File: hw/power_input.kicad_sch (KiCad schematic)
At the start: 24 parts, among them Q101 SQD50P08-25L, Q102 IPD90N10S4-06, U101 TLV3201, U102 UCC27517A

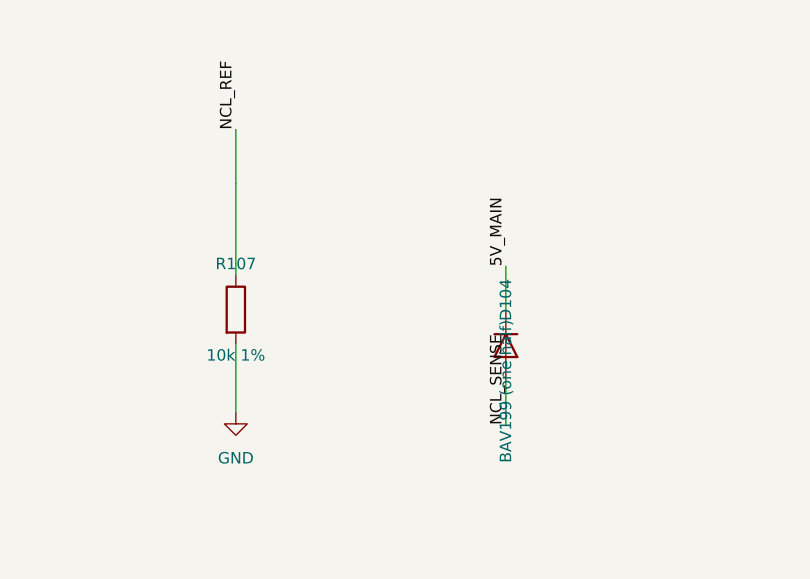
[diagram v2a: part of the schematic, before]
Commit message: Replace the analog-input zeners with BAV199-Q rail clamps
LOWV-CLAMP, analog half. The ten 3.3 V zeners on the sensor and cam
inputs leaked at signal level (the datasheet allows 5 uA at 1 V); they
are now BAV199-Q (80 nA max at 150 C, AEC-Q101) to 3V3_MCU and ground,
drawn as one 3-pin part so each pair is one package. The speed input's
split BAV199 halves and the power-input sense clamp use the same part.

A rail clamp needs something the zener did not: the BAV199's upper
diode is high-Vf, so on a 40 V harness short the MCU pad's ESD diode
would take most of the fault current, over the +/-3 mA injection
limit. Each clamped channel now has 1k between clamp and pad: 0.40 mA
injected. sensor_ratiometric and cam_frontend model the pair, the 1k
and the pad diode, and check the injection current.

The new models also showed the old zener loading the cam signal by
84 mV at a 5.25 V rail -- pinned by the old check as the expected
value. Re-pinned to the divider's own 3.231 V.

The discrete inputs stay open: they clamp continuously, which neither
a rail clamp nor an LM4040-class reference (35 uA bias below
breakdown) can do within the pin's ratings.

24/24 sim blocks, netlist gate passing, 197 R/C packaged.
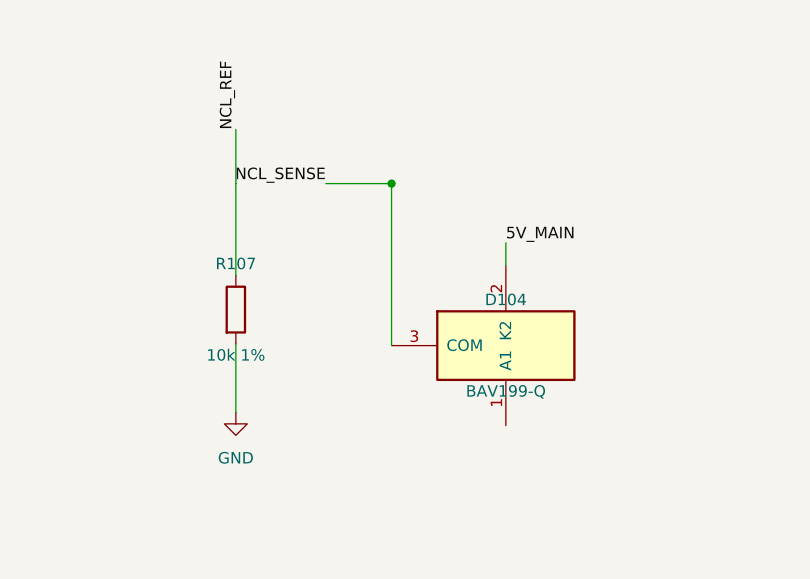
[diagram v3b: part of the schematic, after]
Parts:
- removed D104: BAV199 (one half), symbol Device:D
- added D104: BAV199-Q, Package_TO_SOT_SMD:SOT-23, symbol ecu25kva:BAV199
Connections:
- net 5V_MAIN: now also D104.2 (K2)
- net NCL_SENSE: now also D104.3 (COM)
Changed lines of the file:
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@@
     )
   )
-  (symbol (lib_id "Device:D") (at 190.0 256.0 270) (unit 1)
+  (label "NCL_SENSE" (at 170.0 238.0 180)
+    (effects (font (size 1.27 1.27)) (justify right bottom))
+  )
+  (symbol (lib_id "ecu25kva:BAV199") (at 190.0 256.0 0) (unit 1)
     (in_bom yes) (on_board yes) (fields_autoplaced)
     (property "Reference" "D104" (id 0) (at 190.0 250.92 0)
       (effects (font (size 1.27 1.27)))
     )
-    (property "Value" "BAV199 (one half)" (id 1) (at 190.0 261.08 0)
+    (property "Value" "BAV199-Q" (id 1) (at 190.0 261.08 0)
       (effects (font (size 1.27 1.27)))
     )
-    (property "Footprint" "" (id 2) (at 190.0 256.0 0)
+    (property "Footprint" "Package_TO_SOT_SMD:SOT-23" (id 2) (at 190.0 256.0 0)
       (effects (font (size 1.27 1.27)) hide)
     )
@@
       (effects (font (size 1.27 1.27)) hide)
     )
-    (property "Tag" "VR-CLAMP" (id 4) (at 190.0 256.0 0)
+    (property "MPN" "BAV199-Q" (id 4) (at 190.0 256.0 0)
       (effects (font (size 1.27 1.27)) hide)
     )
-    (property "Note" "Anode to the sense node, cathode to 5V_MAIN: holds the comparator input inside its rail when VIN is at 73.3 V. LOW LEAKAGE for the same reason as on the crank input -- and here leakage lifts the sense node, which makes the clamp release EARLIER, the safe direction." (id 5) (at 190.0 256.0 0)
+    (property "Tag" "VR-CLAMP" (id 5) (at 190.0 256.0 0)
+      (effects (font (size 1.27 1.27)) hide)
+    )
+    (property "Note" "Common pin on the sense node, K2 to 5V_MAIN: holds the comparator input inside its rail when VIN is at 73.3 V. A1 OPEN -- the lower diode would clamp the negative excursion the comparator exists to see. Leakage lifts the sense node, which makes the clamp release EARLIER, the safe direction." (id 6) (at 190.0 256.0 0)
       (effects (font (size 1.27 1.27)) hide)
     )
   )
-  (wire (pts (xy 190.0 252.19) (xy 190.0 247.19))
+  (wire (pts (xy 170.0 238.0) (xy 177.3 238.0))
     (stroke (width 0) (type default))
   )
-  (label "5V_MAIN" (at 190.0 247.19 90)
+  (junction (at 177.3 238.0) (diameter 0) (color 0 0 0 0)
+  )
+  (wire (pts (xy 177.3 238.0) (xy 177.3 256.0))
+    (stroke (width 0) (type default))
+  )
+  (wire (pts (xy 190.0 247.11) (xy 190.0 244.57))
+    (stroke (width 0) (type default))
+  )
+  (label "5V_MAIN" (at 190.0 244.57 0)
     (effects (font (size 1.27 1.27)) (justify left bottom))
   )
-  (wire (pts (xy 190.0 259.81) (xy 190.0 264.81))
-    (stroke (width 0) (type default))
-  )
-  (label "NCL_SENSE" (at 190.0 264.81 270)
-    (effects (font (size 1.27 1.27)) (justify left bottom))
-  )

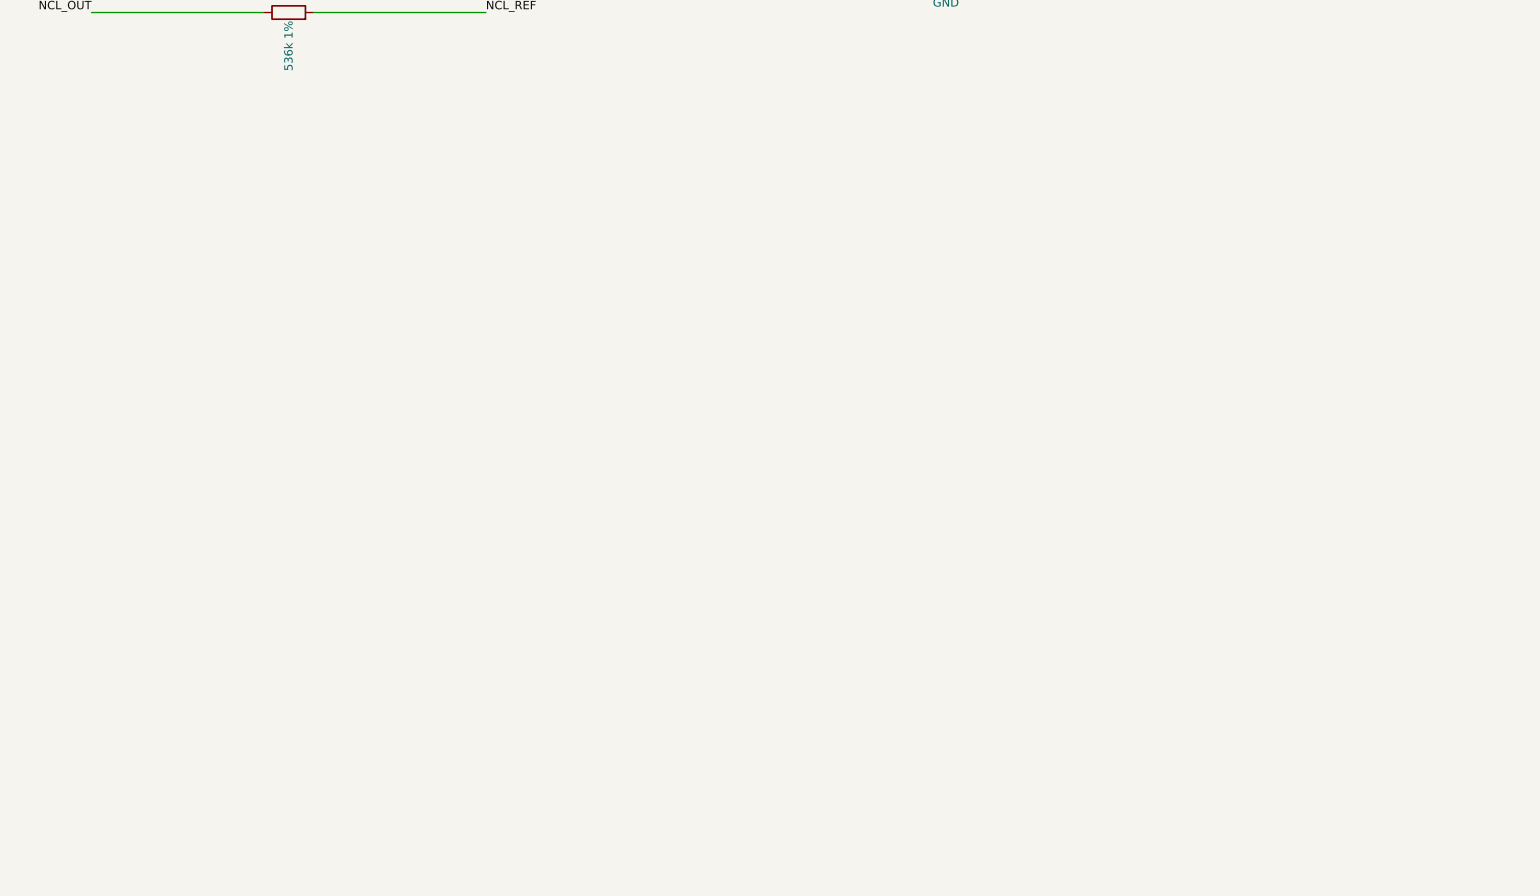
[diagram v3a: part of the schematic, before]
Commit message: Move the injector and EGR supply onto pins 04 and 06 (POWER-PATH)
Every high-current load drew through pin 21, whose reverse FET was
sized for 5 A and whose EMI filter never stated a DC current. Pin 04
now feeds VBAT_INJ (the injector hold switches and the boost power
stage), and pin 06 feeds VBAT_EGR (the EGR bridge). Each is fused 10 A
in the loom and has its own SMCJ43CA TVS, SQM120P10-10m1L reverse
P-FET (passive gate, as Q1), SS20PH102HM3 backstop and 2 x 2.2 uF.
Pin 21 keeps the buck, the relays, the metering freewheel and the
boost controller's VDD.

The pin-21 FET could not simply be copied: at the EGR's 6.4 A stall it
would pass its junction limit on a 105 C board. The new part, from
Vishay doc 76943 Rev. A, runs at Tj 139 C (155 C cranking) on the EGR
rail and 117 C on the injector rail. The new block power_path.cir
holds those figures as 18 checks. check_netlist now fails unless each
rail leaves its own FET for its own loads and VBAT_PROT reaches
neither power stage.

The sheets are generated against KiCad 7.0.11's symbol library, which
regenerates an unchanged sheet identically. KiCad 10's library would
have rewritten every embedded symbol.

Gates: 25/25 blocks; connectivity OK with the same 2 open items; 333
components, 314 with footprints; 208 passives packaged. The questions
put to the owner -- the split, the reverse protection, what stays on
pin 21, and the KiCad/ngspice choices -- are in decisions-log.md
sections 5 and 6. The spec, the BOM requirements, the handbook, status
and the handoff are updated to match, and the bible is rebuilt (333
pages).
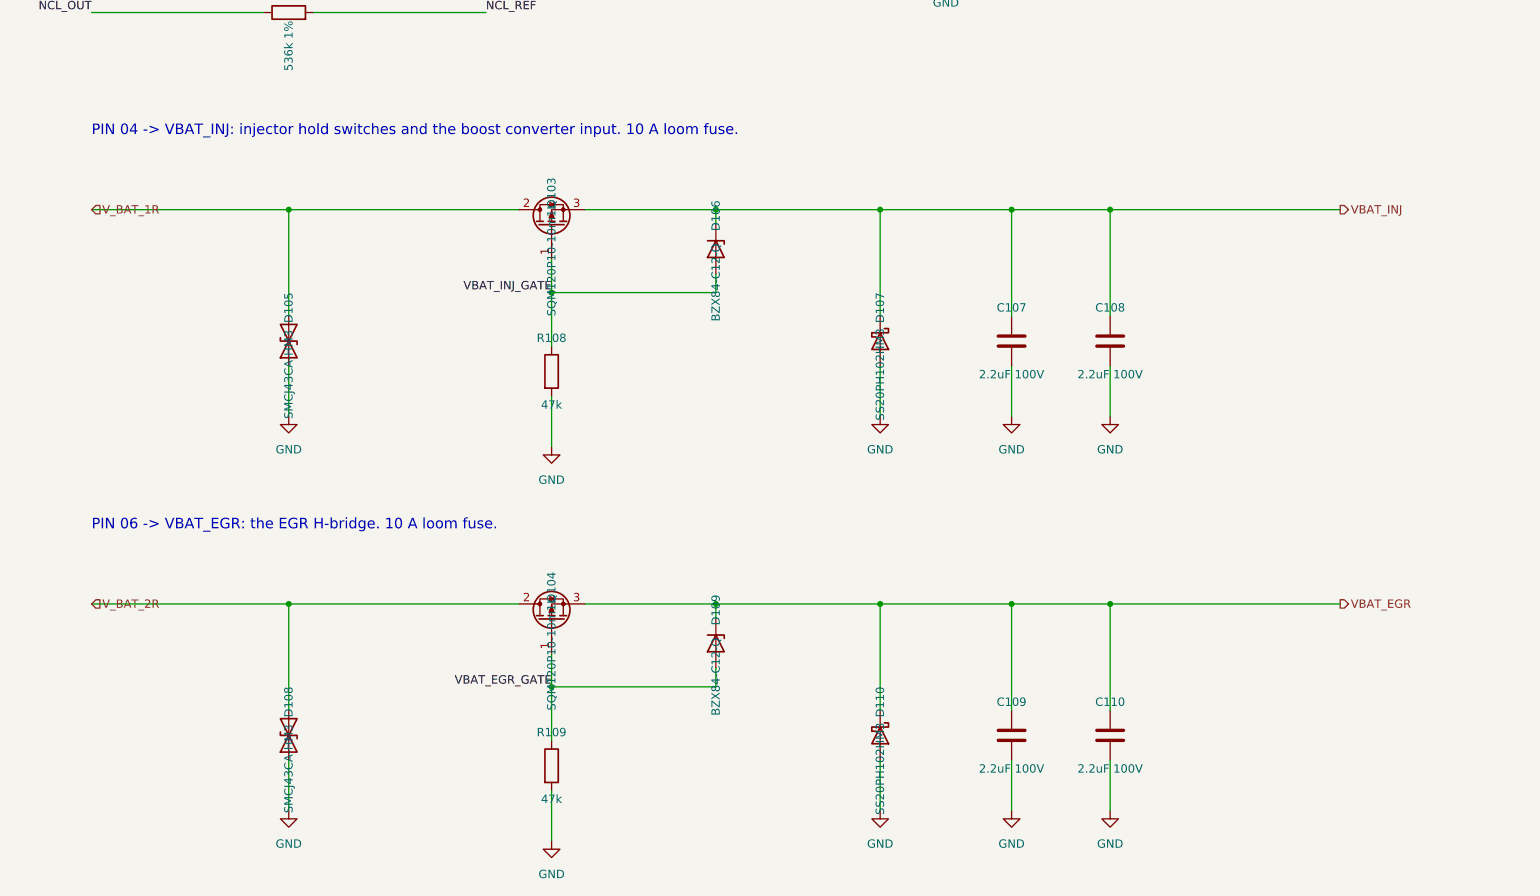
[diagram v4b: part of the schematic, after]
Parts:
- added C107, C108, C109, C110: 2.2uF 100V, Capacitor_SMD:C_1210_3225Metric, symbol Device:C
- added D105, D108: SMCJ43CA-HM3, Diode_SMD:D_SMC, symbol Device:D_TVS
- added D106, D109: BZX84-C12-Q, ecu25kva:SOT-23_Zener_K1_A2, symbol Device:D_Zener
- added D107, D110: SS20PH102HM3, ecu25kva:TO-277A_K1_A2, symbol Device:D_Schottky
- added Q103, Q104: SQM120P10-10m1L, Package_TO_SOT_SMD:TO-263-2, symbol Device:Q_PMOS_GDS
- added R108, R109: 47k, Resistor_SMD:R_0805_2012Metric, symbol Device:R
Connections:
- net GND: now also C107.2, C108.2, C109.2, C110.2, D105.1 (A1), D107.2 (A), D108.1 (A1), D110.2 (A), R108.2, R109.2
- new net VBAT_EGR: C109.1, C110.1, D109.1 (K), D110.1 (K), Q104.3 (S)
- new net VBAT_EGR_GATE: D109.2 (A), Q104.1 (G), R109.1
- new net VBAT_INJ: C107.1, C108.1, D106.1 (K), D107.1 (K), Q103.3 (S)
- new net VBAT_INJ_GATE: D106.2 (A), Q103.1 (G), R108.1
- new net V_BAT_1R: D105.2 (A2), Q103.2 (D)
- new net V_BAT_2R: D108.2 (A2), Q104.2 (D)
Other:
- note added: "PIN 04 -> VBAT_INJ: injector hold switches and the boost converter input. 10 A loom fuse."
- note added: "PIN 06 -> VBAT_EGR: the EGR H-bridge. 10 A loom fuse."

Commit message: Choose pin 21's filter inductors and fuse for its post-POWER-PATH load
With the injector and EGR gone, pin 21 carries at most 2.95 A. That is
an upper bound, not an estimate. The LM5164's IPEAK1 maximum of 1.75 A
(SNVSAU4D) caps the buck's average input current whatever the 5 V load
is. The rest is the two relay coils at 24 V (0.30 A), the metering
freewheel (0.86 A) and the boost VDD feed (0.04 A).

  L101  Wurth 7447709220, 22 uH WE-PD: Isat 6.5 A typ, 117 C at the
        bound on a 105 C board (max 125 C)
  L102  Wurth 744314047, 0.47 uH WE-HCI 7050: Isat 9 A typ
  F101  Littelfuse 0437005.WRA, 5 A 63 V 437A (was 20 A): 3.16 A at
        105 C, 1.07x over the bound

The EMI model now carries both inductors' RDC and self-resonance, and
Lf is 0.47 uH. The 150 and 400 kHz margins fell to 0.56 and 0.73 dB
against the existing placeholder gates. F101's pulse I2t is computed
from the simulated waveforms: pulse 1 is 16% of melting, pulse 2a is
2.5%. The 20% ceiling for the repeated pulse is a rule of thumb, and
the BOM requirements say so. Both land patterns were checked against
the Wurth drawings.

Gates: 25/25 blocks, connectivity OK, 317 of 333 with footprints, 208
passives unchanged. The bible is rebuilt (334 pages).
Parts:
- F101: value 20A -> 0437005.WRA; footprint (none) -> Fuse:Fuse_1206_3216Metric; Chosen (none) -> Littelfuse 437A, 1206 fast-acting, 63 V DC, 50 A interrupti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; Class (none) -> 5A; MPN (none) -> 0437005.WRA; Source spec sec.2.2 -- OEM harness fuse 8F1 class -> run_sim.py emi_filter (pin 21 load), transient_clamp and ne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
- L101: value 22uH -> 7447709220; footprint (none) -> Inductor_SMD:L_Wuerth_WE-PD-Typ-LS; Chosen (none) -> Wurth WE-PD 1210, 22 uH, IR 5.3 A, Isat 6.5 A typ, 28 mOhm 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; Class (none) -> 22uH; MPN (none) -> 7447709220; Source emi_filter.cir L1 -> emi_filter.cir L1 -- RDC and self-resonance modelled
- L102: value 0.5uH -> 744314047; footprint (none) -> Inductor_SMD:L_Wuerth_HCI-7050; Chosen (none) -> Wurth WE-HCI 7050, 0.47 uH, IR 18 A, Isat 9 A typ, 1.35 mOh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; Class (none) -> 0.47uH; MPN (none) -> 744314047; Source emi_filter.cir Lf -> emi_filter.cir Lf -- RDC and self-resonance modelled
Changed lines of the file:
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@@
       (effects (font (size 1.27 1.27)))
     )
-    (property "Value" "20A" (id 1) (at 52 85.08 0)
+    (property "Value" "0437005.WRA" (id 1) (at 52 85.08 0)
       (effects (font (size 1.27 1.27)))
     )
-    (property "Footprint" "" (id 2) (at 52 80.0 0)
+    (property "Footprint" "Fuse:Fuse_1206_3216Metric" (id 2) (at 52 80.0 0)
       (effects (font (size 1.27 1.27)) hide)
     )
@@
       (effects (font (size 1.27 1.27)) hide)
     )
-    (property "Source" "spec sec.2.2 -- OEM harness fuse 8F1 class" (id 4) (at 52 80.0 0)
+    (property "MPN" "0437005.WRA" (id 4) (at 52 80.0 0)
+      (effects (font (size 1.27 1.27)) hide)
+    )
+    (property "Class" "5A" (id 5) (at 52 80.0 0)
+      (effects (font (size 1.27 1.27)) hide)
+    )
+    (property "Chosen" "Littelfuse 437A, 1206 fast-acting, 63 V DC, 50 A interrupting, melting I2t 2.30 A2s, AEC-Q200. 3.16 A continuous at 105 C" (id 6) (at 52 80.0 0)
+      (effects (font (size 1.27 1.27)) hide)
+    )
+    (property "Source" "run_sim.py emi_filter (pin 21 load), transient_clamp and negative_pulses (pulse I2t)" (id 7) (at 52 80.0 0)
       (effects (font (size 1.27 1.27)) hide)
     )
@@
       (effects (font (size 1.27 1.27)))
     )
-    (property "Value" "22uH" (id 1) (at 80 85.08 0)
+    (property "Value" "7447709220" (id 1) (at 80 85.08 0)
       (effects (font (size 1.27 1.27)))
     )
-    (property "Footprint" "" (id 2) (at 80 80.0 0)
+    (property "Footprint" "Inductor_SMD:L_Wuerth_WE-PD-Typ-LS" (id 2) (at 80 80.0 0)
       (effects (font (size 1.27 1.27)) hide)
     )
@@
       (effects (font (size 1.27 1.27)) hide)
     )
-    (property "Source" "emi_filter.cir L1" (id 4) (at 80 80.0 0)
+    (property "MPN" "7447709220" (id 4) (at 80 80.0 0)
+      (effects (font (size 1.27 1.27)) hide)
+    )
+    (property "Class" "22uH" (id 5) (at 80 80.0 0)
+      (effects (font (size 1.27 1.27)) hide)
+    )
+    (property "Chosen" "Wurth WE-PD 1210, 22 uH, IR 5.3 A, Isat 6.5 A typ, 28 mOhm max, SRF 10 MHz, 120 V, AEC-Q200 Grade 1. Land pattern checked against the datasheet's: 2.9 x 5.4 pads, 7.0 gap" (id 6) (at 80 80.0 0)
+      (effects (font (size 1.27 1.27)) hide)
+    )
+    (property "Source" "emi_filter.cir L1 -- RDC and self-resonance modelled" (id 7) (at 80 80.0 0)
       (effects (font (size 1.27 1.27)) hide)
     )
@@
       (effects (font (size 1.27 1.27)))
     )
-    (property "Value" "0.5uH" (id 1) (at 138 85.08 0)
+    (property "Value" "744314047" (id 1) (at 138 85.08 0)
       (effects (font (size 1.27 1.27)))
     )
-    (property "Footprint" "" (id 2) (at 138 80.0 0)
+    (property "Footprint" "Inductor_SMD:L_Wuerth_HCI-7050" (id 2) (at 138 80.0 0)
       (effects (font (size 1.27 1.27)) hide)
     )
@@
       (effects (font (size 1.27 1.27)) hide)
     )
-    (property "Source" "emi_filter.cir Lf" (id 4) (at 138 80.0 0)
+    (property "MPN" "744314047" (id 4) (at 138 80.0 0)
       (effects (font (size 1.27 1.27)) hide)
     )
+    (property "Class" "0.47uH" (id 5) (at 138 80.0 0)
+      (effects (font (size 1.27 1.27)) hide)
+    )
+    (property "Chosen" "Wurth WE-HCI 7050, 0.47 uH, IR 18 A, Isat 9 A typ, 1.35 mOhm, SRF 235 MHz, AEC-Q200 Grade 1. Land pattern checked: 2.7 x 2.2 pads, 2.4 gap" (id 6) (at 138 80.0 0)
+      (effects (font (size 1.27 1.27)) hide)
+    )
+    (property "Source" "emi_filter.cir Lf -- RDC and self-resonance modelled" (id 7) (at 138 80.0 0)
+      (effects (font (size 1.27 1.27)) hide)
+    )
